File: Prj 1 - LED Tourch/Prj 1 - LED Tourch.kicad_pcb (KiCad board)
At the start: 2 copper layers, 67.1 x 19.6 mm, 4 parts, among them SW1 SW_DIP_x01

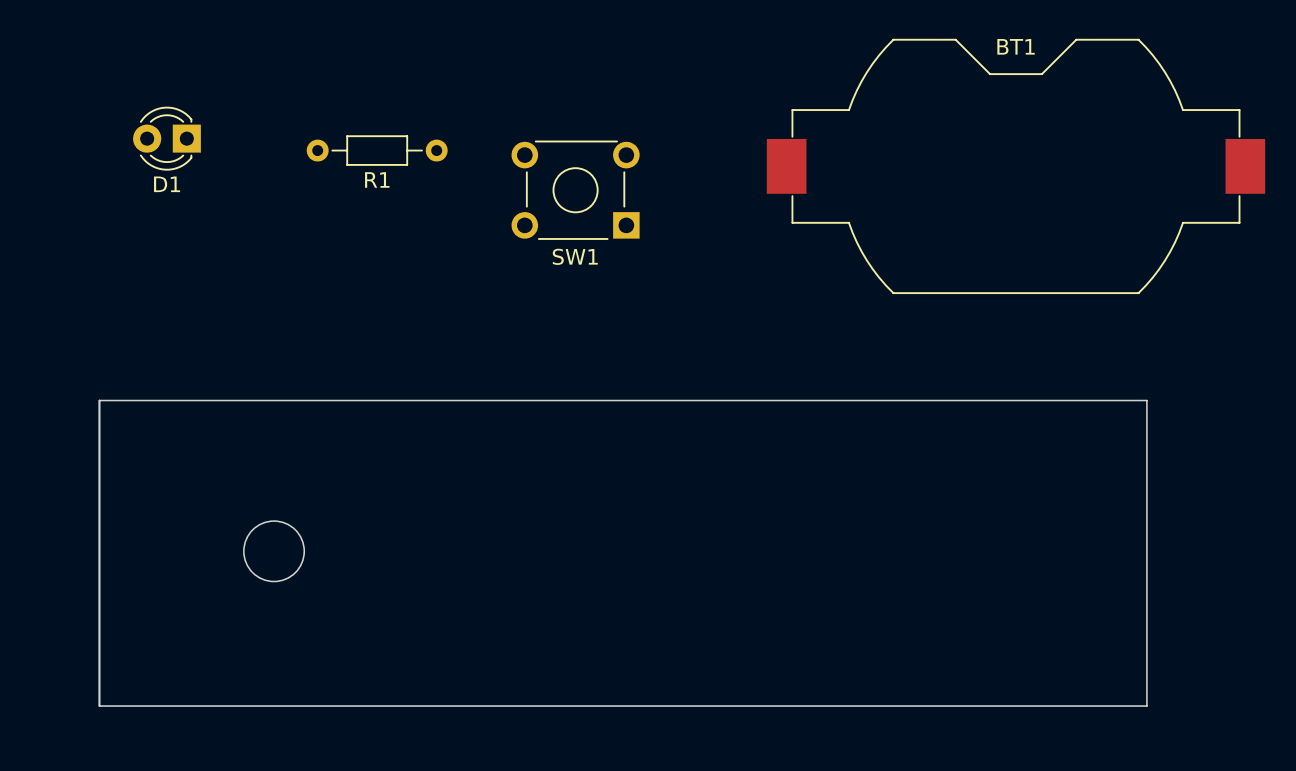
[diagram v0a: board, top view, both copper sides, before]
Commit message: update to include routing
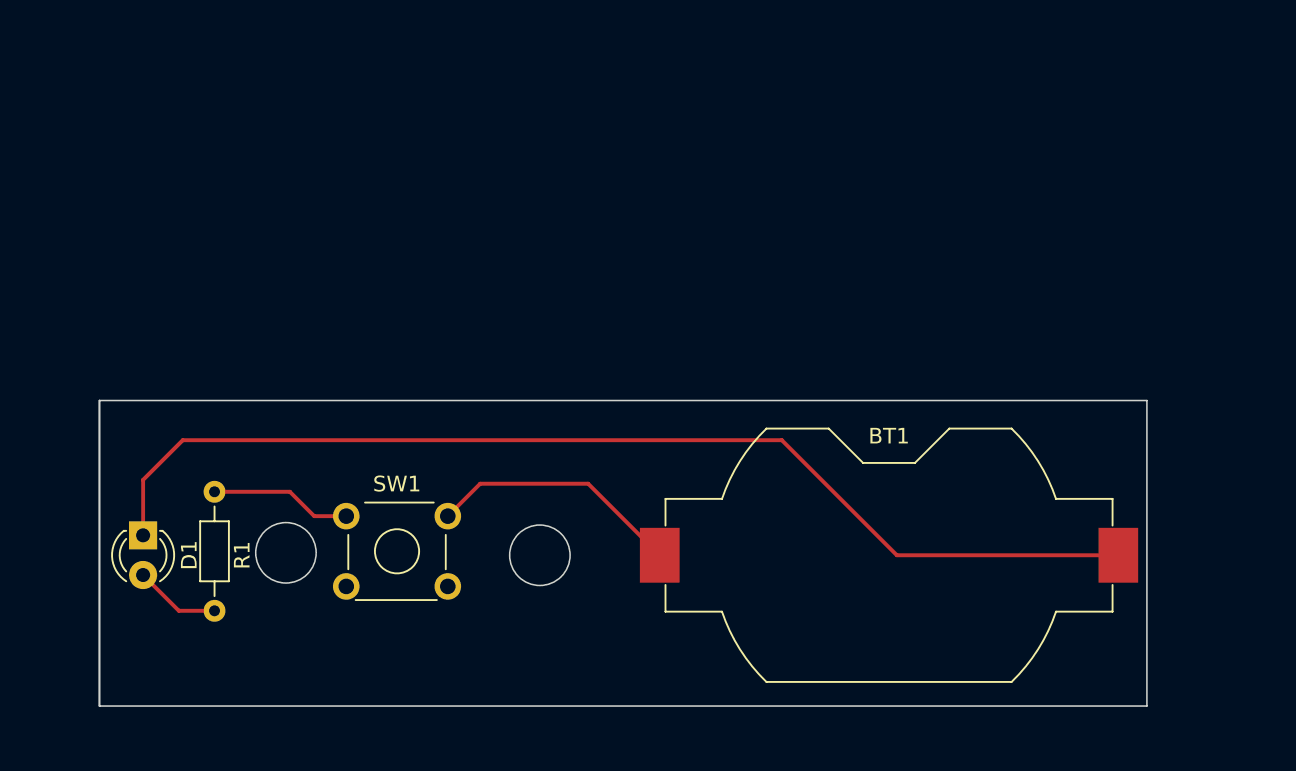
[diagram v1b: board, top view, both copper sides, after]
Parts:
- D1: footprint LED_THT:LED_D3.0mm_IRGrey -> LED_THT:LED_D3.0mm
- SW1: footprint Button_Switch_THT:SW_TH_Tactile_Omron_B3F-10xx -> Library:SW_TH_Tactile_Omron_B3F-10xx_2
- moved BT1 26.2 mm to (152.9, 89.2)
- moved R1 26.1 mm to (109.7, 85.1), turned to -90 degrees
- moved SW1 25.8 mm to (118.2, 86.7), turned to 0 degrees
- moved D1 25.5 mm to (105.2, 87.9), turned to -90 degrees
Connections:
- BT1 pad 1: /bat_pos -> /LED_cathode
- BT1 pad 2: /LED_cathode -> /bat_pos
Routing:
- net /LED_cathode: track 0.00 -> 70.1 mm
- net /bat_pos: track 0.00 -> 16.3 mm
- net Net-(R1-Pad1): track 0.00 -> 9.08 mm
- net /LED_anode: track 0.00 -> 5.52 mm
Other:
- outline, holes or cut-outs redrawn
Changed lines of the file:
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@@
   (net 4 "Net-(R1-Pad1)")
   (footprint "Resistor_THT:R_Axial_DIN0204_L3.6mm_D1.6mm_P7.62mm_Horizontal" (layer "F.Cu")
-    (at 123.952 63.246 180)
+    (at 109.728 85.09 -90)
     (descr "Resistor, Axial_DIN0204 series, Axial, Horizontal, pin pitch=7.62mm, 0.167W, length*diameter=3.6*1.6mm^2, http://cdn-reichelt.de/documents/datenblatt/B400/1_4W%23YAG.pdf")
     (tags "Resistor Axial_DIN0204 series Axial Horizontal pin pitch 7.62mm 0.167W length 3.6mm diameter 1.6mm")
@@
     (property "ki_keywords" "R res resistor")
     (attr through_hole)
-    (fp_text reference "R1" (at 3.81 -1.92) (layer "F.SilkS")
-        (effects (font (size 1 1) (thickness 0.15)))
-    )
-    (fp_text value "R" (at 3.81 1.92) (layer "F.Fab")
-        (effects (font (size 1 1) (thickness 0.15)))
-    )
-    (fp_text user "${REFERENCE}" (at 7.62 0) (layer "F.Fab")
+    (fp_text reference "R1" (at 4.064 -1.778 -270) (layer "F.SilkS")
+        (effects (font (size 1 1) (thickness 0.15)))
+    )
+    (fp_text value "R" (at 4.064 1.524 -270) (layer "F.Fab")
+        (effects (font (size 1 1) (thickness 0.15)))
+    )
+    (fp_text user "${REFERENCE}" (at 7.62 0 -270) (layer "F.Fab")
         (effects (font (size 0.72 0.72) (thickness 0.108)))
     )
@@
     (fp_line (start 7.62 0) (end 5.61 0)
       (stroke (width 0.1) (type solid)) (layer "F.Fab"))
-    (pad "1" thru_hole circle (at 0 0 180) (size 1.4 1.4) (drill 0.7) (layers "*.Cu" "*.Mask")
+    (pad "1" thru_hole circle (at 0 0 270) (size 1.4 1.4) (drill 0.7) (layers "*.Cu" "*.Mask")
       (net 4 "Net-(R1-Pad1)") (pintype "passive"))
-    (pad "2" thru_hole oval (at 7.62 0 180) (size 1.4 1.4) (drill 0.7) (layers "*.Cu" "*.Mask")
+    (pad "2" thru_hole oval (at 7.62 0 270) (size 1.4 1.4) (drill 0.7) (layers "*.Cu" "*.Mask")
       (net 3 "/LED_anode") (pintype "passive"))
     (model "${KICAD6_3DMODEL_DIR}/Resistor_THT.3dshapes/R_Axial_DIN0204_L3.6mm_D1.6mm_P7.62mm_Horizontal.wrl"
@@
     )
   )
-  (footprint "Button_Switch_THT:SW_TH_Tactile_Omron_B3F-10xx" (layer "F.Cu")
-    (at 136.092 68.036 180)
+  (footprint "Library:SW_TH_Tactile_Omron_B3F-10xx_2" (layer "F.Cu")
+    (at 118.162 86.65)
     (descr "SW_TH_Tactile_Omron_B3F-10xx_https://www.omron.com/ecb/products/pdf/en-b3f.pdf")
     (tags "Omron B3F-10xx")
@@
     (fp_line (start 6.25 -0.75) (end 6.25 5.25)
       (stroke (width 0.1) (type solid)) (layer "F.Fab"))
-    (pad "1" thru_hole rect (at 0 0 180) (size 1.7 1.7) (drill 1) (layers "*.Cu" "*.Mask")
+    (pad "1" thru_hole circle (at 0 0) (size 1.7 1.7) (drill 1) (layers "*.Cu" "*.Mask")
       (net 4 "Net-(R1-Pad1)") (pintype "passive"))
-    (pad "1" thru_hole circle (at 6.5 0 180) (size 1.7 1.7) (drill 1) (layers "*.Cu" "*.Mask")
-      (net 4 "Net-(R1-Pad1)") (pintype "passive"))
-    (pad "2" thru_hole circle (at 0 4.5 180) (size 1.7 1.7) (drill 1) (layers "*.Cu" "*.Mask")
+    (pad "2" thru_hole circle (at 6.5 0) (size 1.7 1.7) (drill 1) (layers "*.Cu" "*.Mask")
       (net 1 "/bat_pos") (pintype "passive"))
-    (pad "2" thru_hole circle (at 6.5 4.5 180) (size 1.7 1.7) (drill 1) (layers "*.Cu" "*.Mask")
-      (net 1 "/bat_pos") (pintype "passive"))
+    (pad "3" thru_hole circle (at 0 4.5) (size 1.7 1.7) (drill 1) (layers "*.Cu" "*.Mask"))
+    (pad "4" thru_hole circle (at 6.5 4.5) (size 1.7 1.7) (drill 1) (layers "*.Cu" "*.Mask"))
     (model "${KICAD6_3DMODEL_DIR}/Button_Switch_THT.3dshapes/SW_TH_Tactile_Omron_B3F-10xx.wrl"
       (offset (xyz 0 0 0))
@@
     )
   )
-  (footprint "LED_THT:LED_D3.0mm_IRGrey" (layer "F.Cu")
-    (at 107.955 62.484 180)
-    (descr "IR-LED, diameter 3.0mm, 2 pins, color: grey")
-    (tags "IR infrared LED diameter 3.0mm 2 pins grey")
+  (footprint "LED_THT:LED_D3.0mm" (layer "F.Cu")
+    (at 105.156 87.879 -90)
+    (descr "LED, diameter 3.0mm, 2 pins")
+    (tags "LED diameter 3.0mm 2 pins")
     (property "Sheetfile" "Prj 1 - LED Tourch.kicad_sch")
     (property "Sheetname" "")
@@
     (property "ki_keywords" "LED diode")
     (attr through_hole)
-    (fp_text reference "D1" (at 1.27 -2.96 180) (layer "F.SilkS")
-        (effects (font (size 1 1) (thickness 0.15)))
-    )
-    (fp_text value "LED" (at 1.27 2.96 180) (layer "F.Fab")
-        (effects (font (size 1 1) (thickness 0.15)))
-    )
-    (fp_text user "${REFERENCE}" (at 1.47 0 180) (layer "F.Fab")
-        (effects (font (size 0.8 0.8) (thickness 0.12)))
+    (fp_text reference "D1" (at 1.27 -2.96 90) (layer "F.SilkS")
+        (effects (font (size 1 1) (thickness 0.15)))
+    )
+    (fp_text value "LED" (at 1.27 2.96 90) (layer "F.Fab")
+        (effects (font (size 1 1) (thickness 0.15)))
     )
     (fp_line (start -0.29 -1.236) (end -0.29 -1.08)
@@
     (fp_circle (center 1.27 0) (end 2.77 0)
       (stroke (width 0.1) (type solid)) (fill none) (layer "F.Fab"))
-    (pad "1" thru_hole rect (at 0 0 180) (size 1.8 1.8) (drill 0.9) (layers "*.Cu" "*.Mask")
+    (pad "1" thru_hole rect (at 0 0 270) (size 1.8 1.8) (drill 0.9) (layers "*.Cu" "*.Mask")
       (net 2 "/LED_cathode") (pinfunction "K") (pintype "passive"))
-    (pad "2" thru_hole circle (at 2.54 0 180) (size 1.8 1.8) (drill 0.9) (layers "*.Cu" "*.Mask")
+    (pad "2" thru_hole circle (at 2.54 0 270) (size 1.8 1.8) (drill 0.9) (layers "*.Cu" "*.Mask")
       (net 3 "/LED_anode") (pinfunction "A") (pintype "passive"))
-    (model "${KICAD6_3DMODEL_DIR}/LED_THT.3dshapes/LED_D3.0mm_IRGrey.wrl"
+    (model "${KICAD6_3DMODEL_DIR}/LED_THT.3dshapes/LED_D3.0mm.wrl"
       (offset (xyz 0 0 0))
       (scale (xyz 1 1 1))
@@
   )
   (footprint "Battery:BatteryHolder_Keystone_1058_1x2032" (layer "F.Cu")
-    (at 161.036 64.262 180)
+    (at 152.908 89.154 180)
     (descr "http://www.keyelco.com/product-pdf.cfm?p=14028")
     (tags "Keystone type 1058 coin cell retainer")
@@
       (stroke (width 0.1) (type solid)) (layer "F.Fab"))
     (pad "1" smd rect (at -14.68 0 180) (size 2.54 3.51) (layers "F.Cu" "F.Paste" "F.Mask")
-      (net 1 "/bat_pos") (pinfunction "+") (pintype "passive"))
+      (net 2 "/LED_cathode") (pinfunction "+") (pintype "passive"))
     (pad "2" smd rect (at 14.68 0 180) (size 2.54 3.51) (layers "F.Cu" "F.Paste" "F.Mask")
-      (net 2 "/LED_cathode") (pinfunction "-") (pintype "passive"))
+      (net 1 "/bat_pos") (pinfunction "-") (pintype "passive"))
     (model "${KICAD6_3DMODEL_DIR}/Battery.3dshapes/BatteryHolder_Keystone_1058_1x2032.wrl"
       (offset (xyz 0 0 0))
@@
   (gr_line (start 169.418 79.248) (end 102.362 79.248)
     (stroke (width 0.1) (type default)) (layer "Edge.Cuts"))
+  (gr_circle (center 130.556 89.154) (end 132.490406 89.154)
+    (stroke (width 0.1) (type default)) (fill none) (layer "Edge.Cuts"))
   (gr_line (start 102.362 98.806) (end 169.418 98.806)
     (stroke (width 0.1) (type default)) (layer "Edge.Cuts"))
-  (gr_circle (center 113.538 88.9) (end 112.776 90.678)
+  (gr_circle (center 114.3 88.997594) (end 116.234406 88.997594)
     (stroke (width 0.1) (type default)) (fill none) (layer "Edge.Cuts"))
   (gr_line (start 102.362 79.248) (end 102.362 98.806)
@@
   (gr_line (start 102.362 79.248) (end 102.362 98.806)
     (stroke (width 0.1) (type default)) (layer "Edge.Cuts"))
-  (gr_circle (center 113.538 88.9) (end 115.316 89.662)
-    (stroke (width 0.15) (type default)) (fill none) (layer "User.1"))
-  (gr_rect (start 102.362 79.248) (end 169.418 99.06)
-    (stroke (width 0.15) (type default)) (fill none) (layer "User.1"))
+  (segment (start 133.648 84.574) (end 126.738 84.574) (width 0.25) (layer "F.Cu") (net 1))
+  (segment (start 133.648 84.574) (end 138.228 89.154) (width 0.25) (layer "F.Cu") (net 1))
+  (segment (start 126.738 84.574) (end 124.662 86.65) (width 0.25) (layer "F.Cu") (net 1))
+  (segment (start 153.416 89.154) (end 167.588 89.154) (width 0.25) (layer "F.Cu") (net 2))
+  (segment (start 146.05 81.788) (end 153.416 89.154) (width 0.25) (layer "F.Cu") (net 2))
+  (segment (start 105.156 87.879) (end 105.156 84.328) (width 0.25) (layer "F.Cu") (net 2))
+  (segment (start 107.696 81.788) (end 146.05 81.788) (width 0.25) (layer "F.Cu") (net 2))
+  (segment (start 105.156 84.328) (end 107.696 81.788) (width 0.25) (layer "F.Cu") (net 2))
+  (segment (start 107.447 92.71) (end 109.728 92.71) (width 0.25) (layer "F.Cu") (net 3))
+  (segment (start 105.156 90.419) (end 107.447 92.71) (width 0.25) (layer "F.Cu") (net 3))
+  (segment (start 116.114 86.65) (end 118.162 86.65) (width 0.25) (layer "F.Cu") (net 4))
+  (segment (start 114.554 85.09) (end 116.114 86.65) (width 0.25) (layer "F.Cu") (net 4))
+  (segment (start 109.728 85.09) (end 114.554 85.09) (width 0.25) (layer "F.Cu") (net 4))
 )

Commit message: cut the edge for the battery
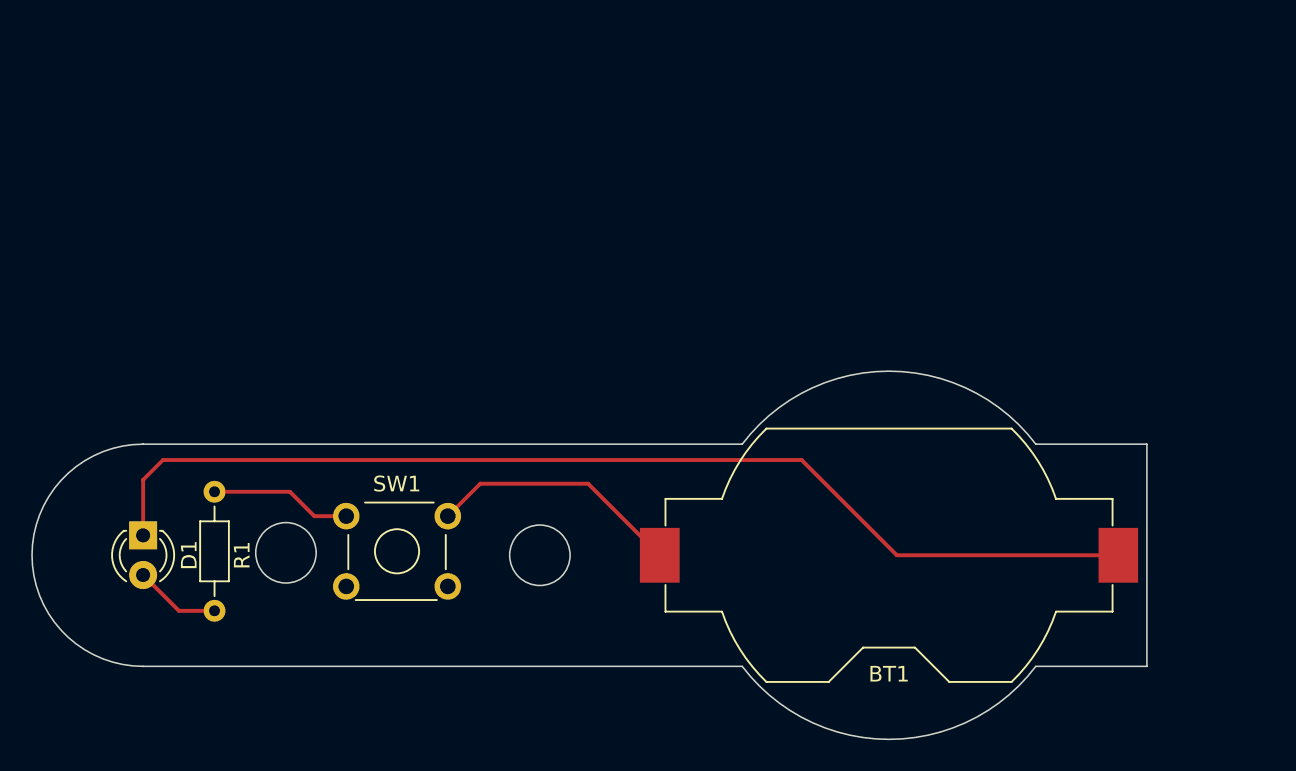
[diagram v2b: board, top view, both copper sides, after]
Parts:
- turned BT1 to 0 degrees
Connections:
- BT1 pad 1: /LED_cathode -> /bat_pos
- BT1 pad 2: /bat_pos -> /LED_cathode
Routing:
- net /LED_cathode: track 70.1 -> 69.0 mm
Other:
- board size 67.1 x 19.6 mm -> 71.4 x 23.6 mm
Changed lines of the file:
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@@
   )
   (footprint "Battery:BatteryHolder_Keystone_1058_1x2032" (layer "F.Cu")
-    (at 152.908 89.154 180)
+    (at 152.908 89.154)
     (descr "http://www.keyelco.com/product-pdf.cfm?p=14028")
     (tags "Keystone type 1058 coin cell retainer")
@@
     (fp_arc (start 10.61275 3.5) (mid 9.478596 5.919179) (end 7.802602 7.999992)
       (stroke (width 0.1) (type solid)) (layer "F.Fab"))
-    (pad "1" smd rect (at -14.68 0 180) (size 2.54 3.51) (layers "F.Cu" "F.Paste" "F.Mask")
-      (net 2 "/LED_cathode") (pinfunction "+") (pintype "passive"))
-    (pad "2" smd rect (at 14.68 0 180) (size 2.54 3.51) (layers "F.Cu" "F.Paste" "F.Mask")
-      (net 1 "/bat_pos") (pinfunction "-") (pintype "passive"))
+    (pad "1" smd rect (at -14.68 0) (size 2.54 3.51) (layers "F.Cu" "F.Paste" "F.Mask")
+      (net 1 "/bat_pos") (pinfunction "+") (pintype "passive"))
+    (pad "2" smd rect (at 14.68 0) (size 2.54 3.51) (layers "F.Cu" "F.Paste" "F.Mask")
+      (net 2 "/LED_cathode") (pinfunction "-") (pintype "passive"))
     (model "${KICAD6_3DMODEL_DIR}/Battery.3dshapes/BatteryHolder_Keystone_1058_1x2032.wrl"
       (offset (xyz 0 0 0))
@@
     )
   )
-  (gr_line (start 169.418 79.248) (end 102.362 79.248)
+  (gr_arc (start 143.51 82.042) (mid 152.908 77.368291) (end 162.306 82.042)
+    (stroke (width 0.1) (type default)) (layer "Edge.Cuts"))
+  (gr_arc (start 162.306 96.266) (mid 152.908 100.939709) (end 143.51 96.266)
+    (stroke (width 0.1) (type default)) (layer "Edge.Cuts"))
+  (gr_line (start 143.51 82.042) (end 105.156 82.042)
     (stroke (width 0.1) (type default)) (layer "Edge.Cuts"))
   (gr_circle (center 130.556 89.154) (end 132.490406 89.154)
     (stroke (width 0.1) (type default)) (fill none) (layer "Edge.Cuts"))
-  (gr_line (start 102.362 98.806) (end 169.418 98.806)
+  (gr_arc (start 105.156 96.266) (mid 98.044 89.154) (end 105.156 82.042)
+    (stroke (width 0.1) (type default)) (layer "Edge.Cuts"))
+  (gr_line (start 162.306 96.266) (end 169.418 96.266)
+    (stroke (width 0.1) (type default)) (layer "Edge.Cuts"))
+  (gr_line (start 105.156 96.266) (end 143.51 96.266)
     (stroke (width 0.1) (type default)) (layer "Edge.Cuts"))
   (gr_circle (center 114.3 88.997594) (end 116.234406 88.997594)
     (stroke (width 0.1) (type default)) (fill none) (layer "Edge.Cuts"))
-  (gr_line (start 102.362 79.248) (end 102.362 98.806)
+  (gr_line (start 169.418 96.266) (end 169.418 82.042)
     (stroke (width 0.1) (type default)) (layer "Edge.Cuts"))
-  (gr_line (start 169.418 98.806) (end 169.418 79.248)
-    (stroke (width 0.1) (type default)) (layer "Edge.Cuts"))
-  (gr_line (start 102.362 79.248) (end 102.362 98.806)
+  (gr_line (start 169.418 82.042) (end 162.306 82.042)
     (stroke (width 0.1) (type default)) (layer "Edge.Cuts"))
   (segment (start 133.648 84.574) (end 126.738 84.574) (width 0.25) (layer "F.Cu") (net 1))
@@
   (segment (start 126.738 84.574) (end 124.662 86.65) (width 0.25) (layer "F.Cu") (net 1))
   (segment (start 153.416 89.154) (end 167.588 89.154) (width 0.25) (layer "F.Cu") (net 2))
-  (segment (start 146.05 81.788) (end 153.416 89.154) (width 0.25) (layer "F.Cu") (net 2))
+  (segment (start 147.32 83.058) (end 153.416 89.154) (width 0.25) (layer "F.Cu") (net 2))
   (segment (start 105.156 87.879) (end 105.156 84.328) (width 0.25) (layer "F.Cu") (net 2))
-  (segment (start 107.696 81.788) (end 146.05 81.788) (width 0.25) (layer "F.Cu") (net 2))
-  (segment (start 105.156 84.328) (end 107.696 81.788) (width 0.25) (layer "F.Cu") (net 2))
+  (segment (start 105.156 84.328) (end 106.426 83.058) (width 0.25) (layer "F.Cu") (net 2))
+  (segment (start 106.426 83.058) (end 147.32 83.058) (width 0.25) (layer "F.Cu") (net 2))
   (segment (start 107.447 92.71) (end 109.728 92.71) (width 0.25) (layer "F.Cu") (net 3))
   (segment (start 105.156 90.419) (end 107.447 92.71) (width 0.25) (layer "F.Cu") (net 3))
